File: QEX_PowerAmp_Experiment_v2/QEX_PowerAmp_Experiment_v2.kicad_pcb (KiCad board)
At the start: 4 copper layers, 87 x 74 mm, 91 parts, among them J1 Conn_01x02, J10 Conn_01x03, J11 Conn_01x03, J12 SMA, J13 Conn_01x02, J14 SMA, J2 Key In, J3 Conn_01x02, J4 Key In, J5 SMA, J6 Conn_01x03, J7 Conn_01x02, J8 Conn_01x03, J9 Conn_01x03, Q1 DMN10H220LPDW, Q2 BC847BS, U1 TLV61047DDC, U2 OPA1678, U3 74LVC2G125, U4 MIC5235-3.3YM5, U5 LMR51430, U6 UCC27517DBVR, U7 UCC27517DBVR, U8 LMR51430

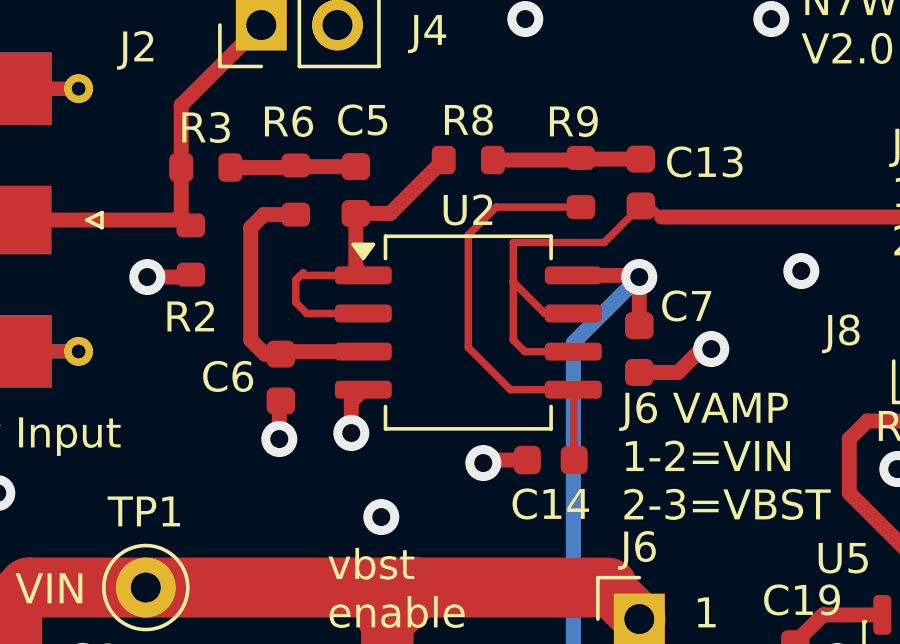
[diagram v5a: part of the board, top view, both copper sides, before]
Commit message: Corrected U2 footprint for jlcpcb; re-submitting
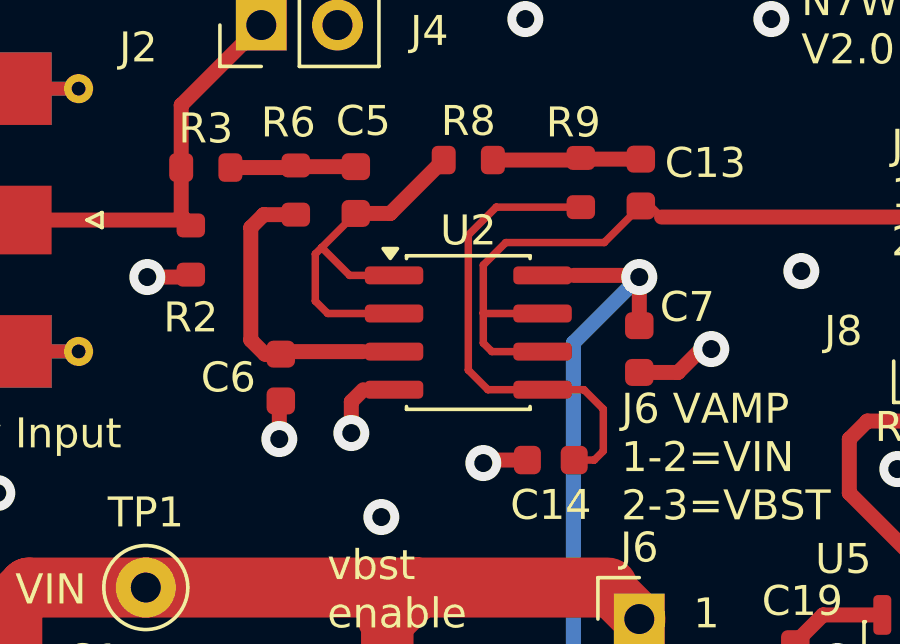
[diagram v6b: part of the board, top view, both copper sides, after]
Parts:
- U2: footprint Package_SO:SOIC-8_5.3x6.2mm_P1.27mm -> Package_SO:SOIC-8_3.9x4.9mm_P1.27mm
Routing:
- net /k5: track 14.3 -> 16.2 mm
- net /k3: track 11.7 -> 12.7 mm
